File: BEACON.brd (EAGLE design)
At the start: 79 x 48 mm, 21 parts, among them IC1 SPARKCORE, IC2 TX-C1FLAT, IC3 RXB1SHORTFLAT, T1 BPX81

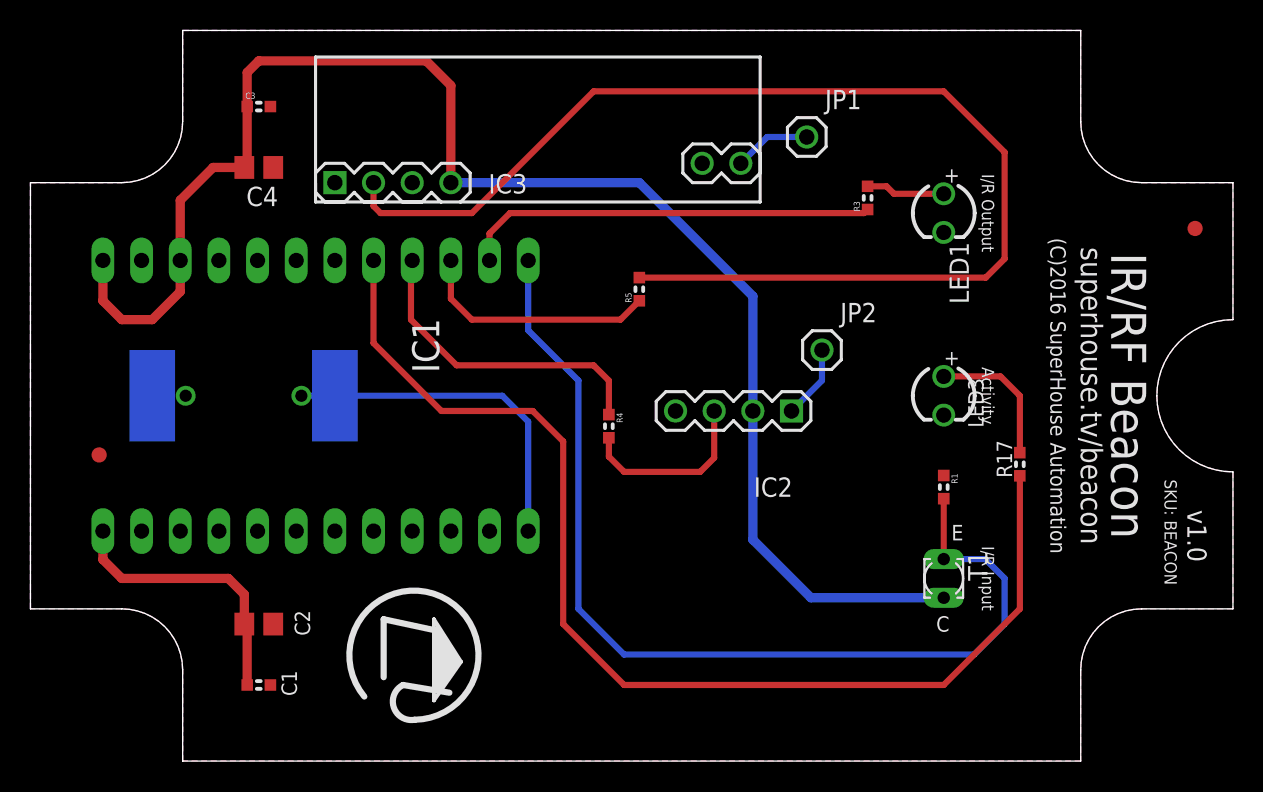
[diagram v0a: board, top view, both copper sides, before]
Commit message: Reduced PCB outline and added action button to initiate binding
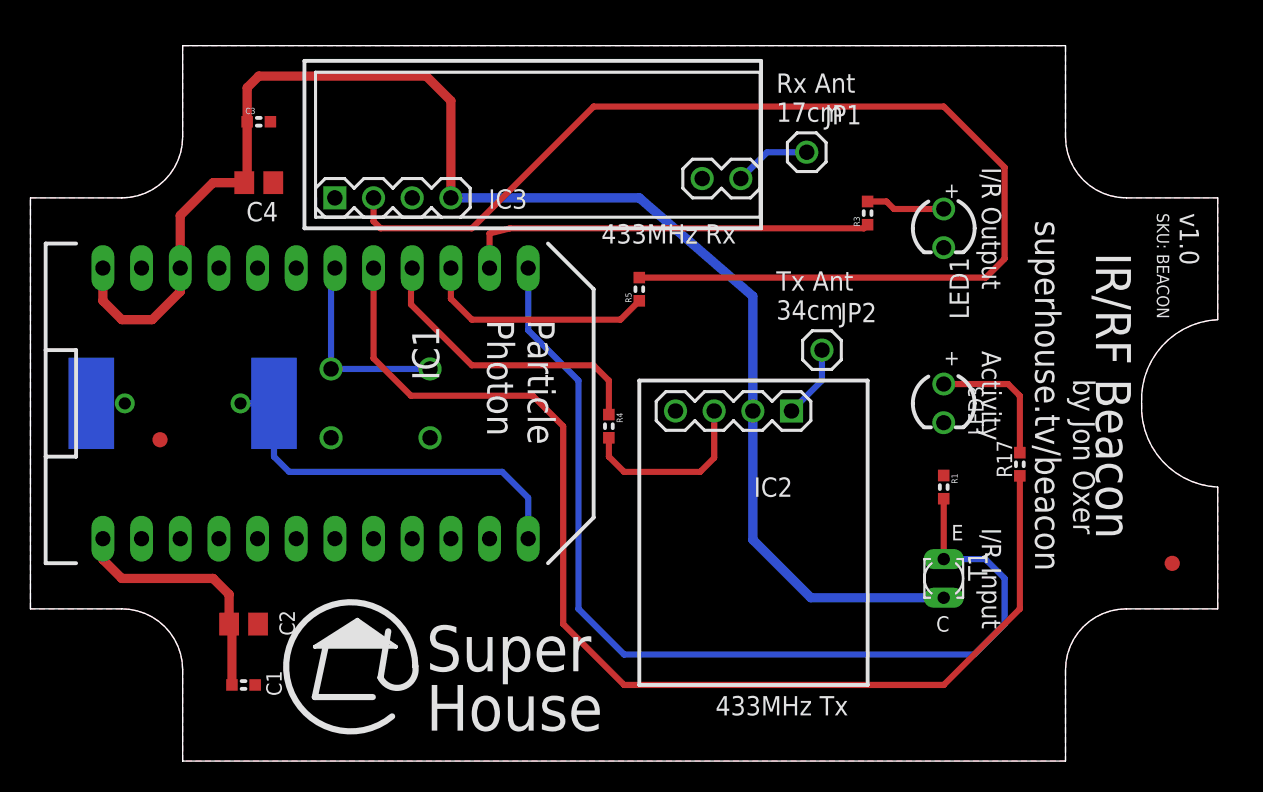
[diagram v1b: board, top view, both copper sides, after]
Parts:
- added S1: SETUP, freetronics-original:TACTILE-PTH
- LED3: value YELLOW 3mm -> GREEN 3mm
- moved U$5 22.1 mm to (75.0, 13.0)
- moved U$4 4.12 mm to (8.51, 21.1)
- moved PIEZO1 4.03 mm to (10.0, 23.5)
- moved PIEZO2 4.03 mm to (10.0, 23.5)
- moved C1 1.00 mm to (14.0, 5.00)
- moved C2 1.00 mm to (14.0, 9.00)
- moved C3 1.00 mm to (15.0, 42.0)
- moved C4 1.00 mm to (15.0, 38.0)
- moved IC3 1.00 mm to (20.0, 37.0)
- moved JP1 1.00 mm to (51.0, 40.0)
- moved LED1 1.00 mm to (60.0, 35.0)
- moved R3 1.00 mm to (55.0, 36.0)
- moved IC1 0.50 mm to (20.0, 23.5)
- moved LED3 0.50 mm to (60.0, 23.5)
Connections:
- new net D5_SETUP: IC1.P$6, S1.3, S1.4
- net GND: now also S1.1, S1.2
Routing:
- net D5_SETUP: track 0.00 -> 13.7 mm
- net A0_PIEZO: track 22.8 -> 26.2 mm
- net VCC: track 100.2 -> 98.0 mm
- net 5V: track 18.1 -> 16.6 mm
- net N$13: track 79.7 -> 78.7 mm
- net D4_LED: track 75.0 -> 75.7 mm
- net D2_RFRX: track 16.0 -> 15.5 mm
- net D0_IRRX: track 65.8 -> 65.3 mm
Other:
- board size 79 x 48 mm -> 78 x 47 mm
- board text added: "(C)2016 SuperHouse Automation Released under the TAPR Open Hardware License www.tapr.org/OHL"
- board text added: "433MHz Rx"
- board text added: "433MHz Tx"
- board text added: "Particle Photon"
- board text added: "Rx Ant 17cm"
- board text added: "Super House"
- board text added: "Tx Ant 34cm"
- board text added: "by Jon Oxer"
- board text removed: "(C)2016 SuperHouse Automation"

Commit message: Added mechanical details
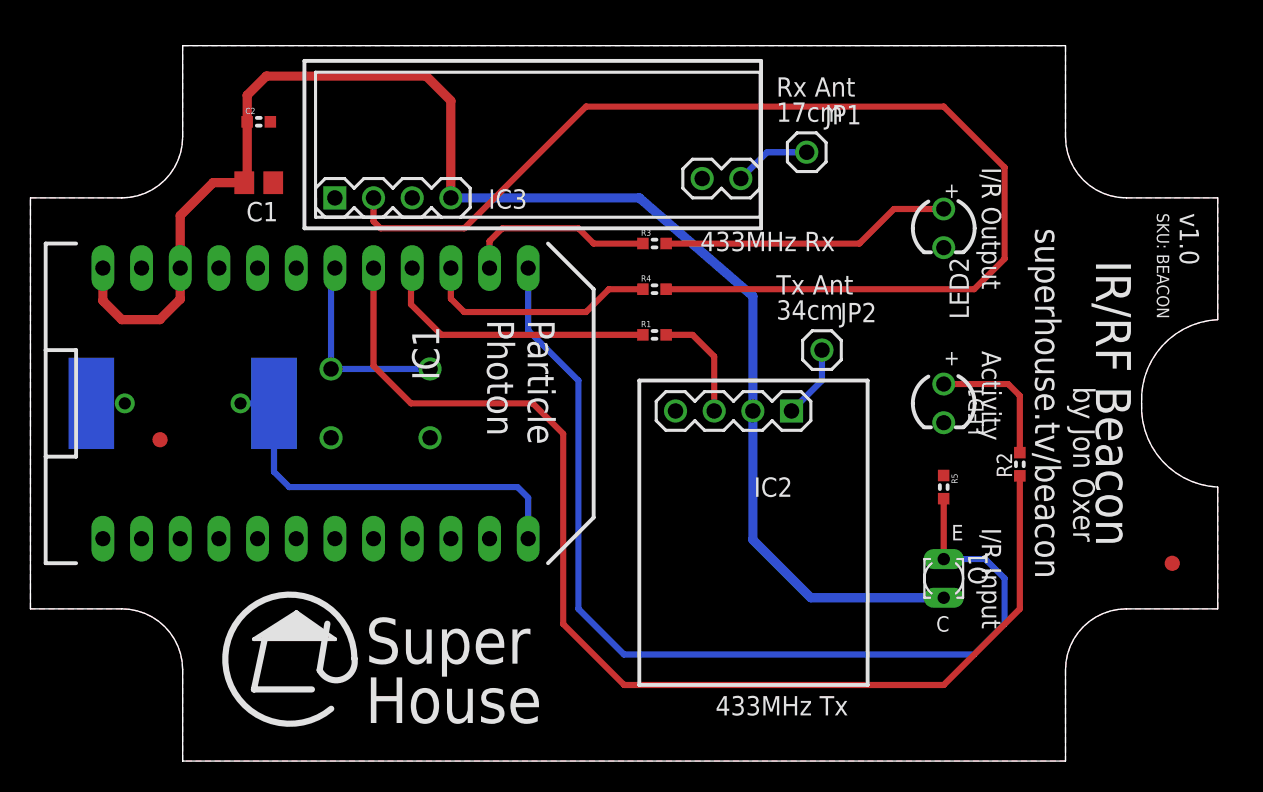
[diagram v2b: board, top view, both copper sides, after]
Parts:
- removed C3: 100nF 0603, freetronics:0603
- removed C4: 10uF 0805, freetronics-jon:C0805
- removed LED3: GREEN 3mm, freetronics-2:LED3MM
- added LED2: IR 3mm, freetronics-2:LED3MM
- C1: value 100nF 0603 -> 10uF; device freetronics:0603 -> freetronics-jon:C0805
- C2: value 10uF 0805 -> 100nF; device freetronics-jon:C0805 -> freetronics:0603
- LED1: value IR 3mm -> GREEN 3mm
- R1, R4, R5: value 1K 0603 -> 1K
- R2: value 470R 0603 -> 470R
- R3: value 100R 0603 -> 100R
- moved C1 33.0 mm to (15.0, 38.0), turned to 180 degrees
- moved C2 33.0 mm to (15.0, 42.0), turned to 0 degrees
- moved R5 23.9 mm to (60.0, 18.0), turned to 270 degrees
- moved R1 21.5 mm to (41.0, 28.0), turned to 0 degrees
- moved R3 14.1 mm to (41.0, 34.0), turned to 0 degrees
- moved LED1 11.5 mm to (60.0, 23.5)
- moved R4 9.49 mm to (41.0, 31.0), turned to 0 degrees
- renumbered R17 to R2, T1 to Q1
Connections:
- removed net 5V: C1.1, C2.2, IC1.P$13
- net D0_IRRX: now also R5.2; no longer R1.2
- net D2_RFRX: now also R4.1; no longer R5.1
- net D3_RFTX: now also R1.1; no longer R4.1
- net GND: now also C1.1, C2.2, LED2.K, R5.1; no longer C1.2, C2.1, C3.2, C4.1, LED3.K, R1.1
- net N$1: now also LED1.A; no longer LED3.A
- net N$13: now also R4.2; no longer R5.2
- net N$2: now also R1.2; no longer R4.2
- net N$3: now also LED2.A; no longer LED1.A
- net VCC: now also C1.2, C2.1; no longer C3.1, C4.2
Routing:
- net 5V: track 16.6 -> 0.00 mm
- net D1_IRTX: track 27.3 -> 12.6 mm
- net N$3: track 5.20 -> 19.2 mm
- net N$2: track 12.1 -> 7.41 mm
- net N$13: track 78.7 -> 77.2 mm
- net D3_RFTX: track 20.5 -> 19.3 mm
- net A0_PIEZO: track 26.2 -> 26.8 mm
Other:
- board text added: "(C)2018 SuperHouse Automation Released under the TAPR Open Hardware License www.tapr.org/OHL"
- board text added: "D0: IR Receiver D1: IR Transmitter D2: 433MHz RF Receiver D3: 433MHz RF Transmitter D4: Activity LED D5: Setup button A0: Piezo"
- board text added: "Setup"
- board text removed: "(C)2016 SuperHouse Automation Released under the TAPR Open Hardware License www.tapr.org/OHL"
- board text removed: "D0: IR Receiver D1: IR Transmitter D2: RF Receiver D3: RF Transmitter D4: Activity LED A0: Piezo"
